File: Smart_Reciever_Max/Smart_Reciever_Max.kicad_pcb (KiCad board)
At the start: 2 copper layers, 112 x 81 mm, 66 parts, among them J1 String1, J10 String10, J11 String11, J12 String12, J13 RJ45, J14 VIN_Voltage, J15 PRG, J2 String2, J3 String3, J4 String4, J5 String5, J6 String6, J7 String7, J8 String8, J9 String9, SW1 SW_Push, U1 AMS1117-3.3, U2 L7805, U3 STM32F410CBTx, U4 AM26LV32xD, U5 74LS125, U6 74LS125, U7 74LS125

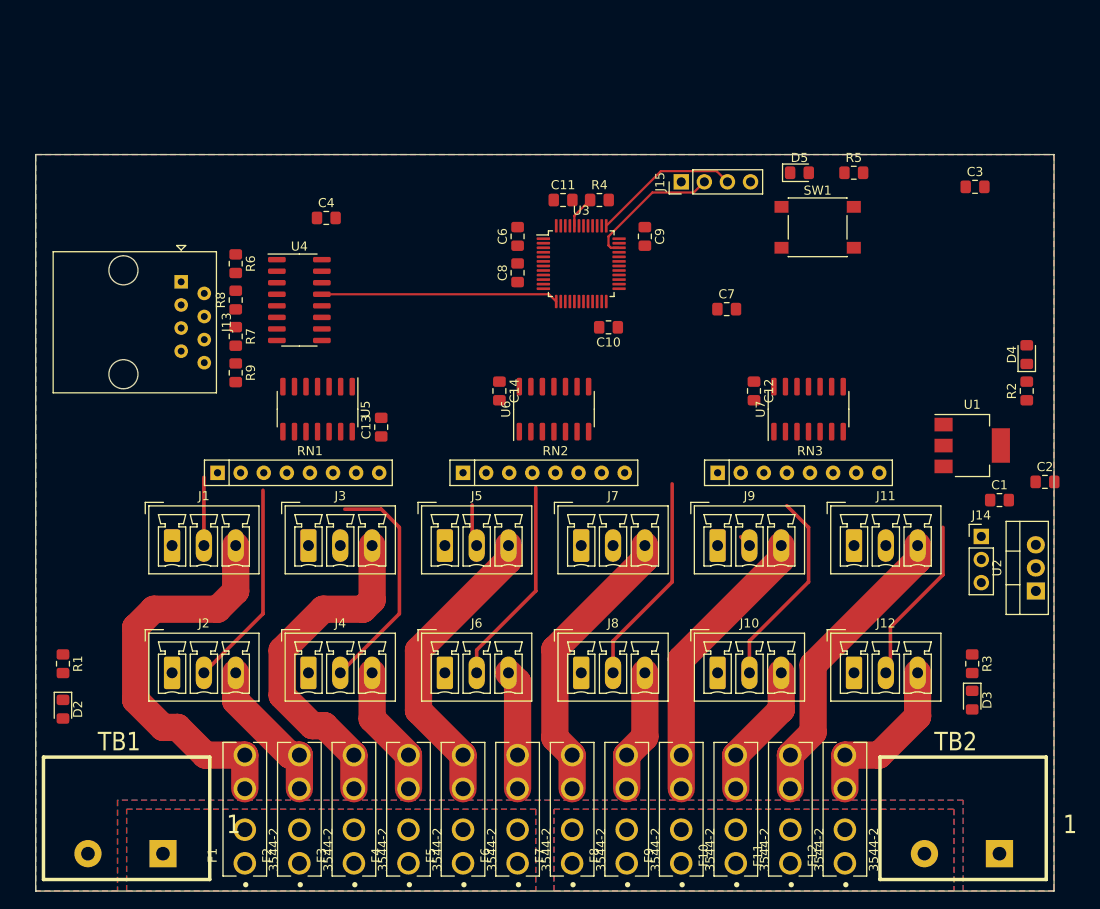
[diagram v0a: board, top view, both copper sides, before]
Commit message: Early Design of 12 port Smart Receiver. TODO: BOM, and clean up firmware for STM32L412
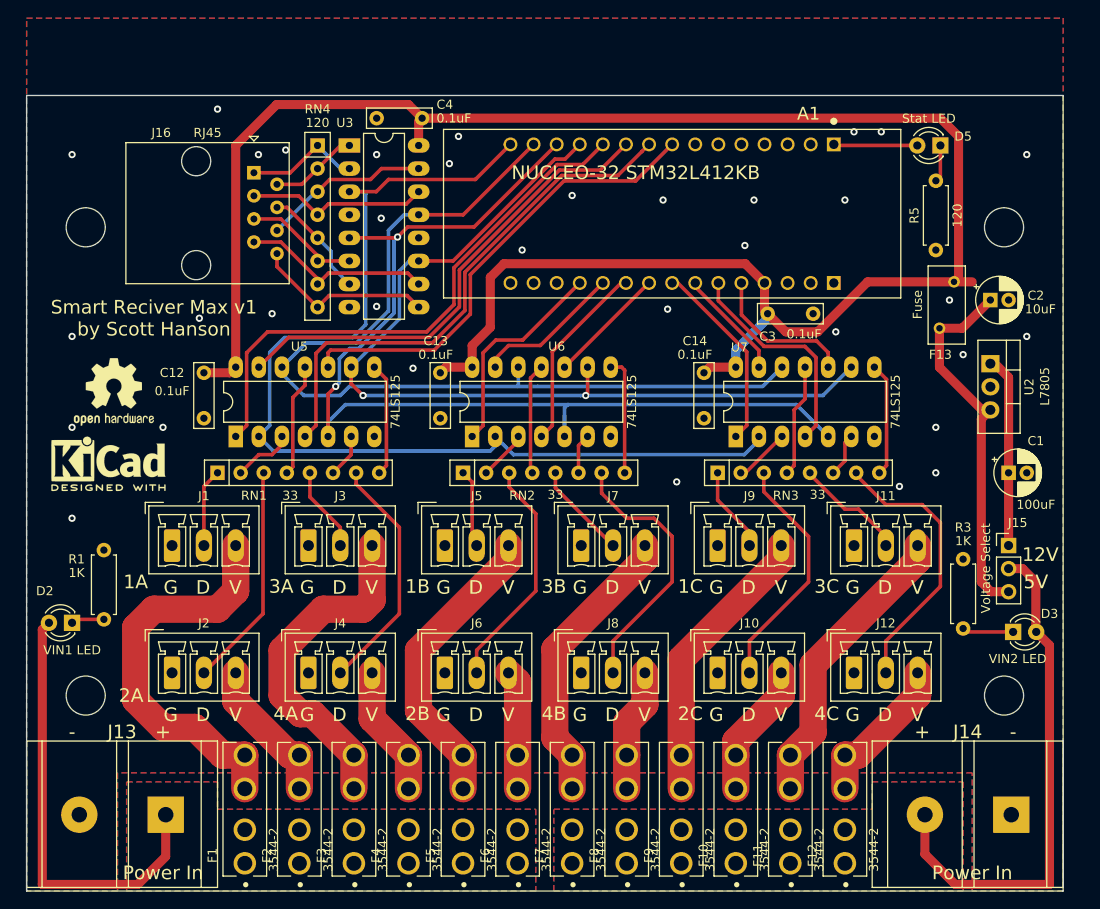
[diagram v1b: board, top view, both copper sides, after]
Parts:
- removed C10, C11, C6, C8, C9: 0.1uF, Capacitor_SMD:C_0805_2012Metric_Pad1.15x1.40mm_HandSolder
- removed C7: 4.7uF, Capacitor_SMD:C_0805_2012Metric_Pad1.15x1.40mm_HandSolder
- removed D4: 3.3V LED, LED_SMD:LED_0805_2012Metric_Pad1.15x1.40mm_HandSolder
- removed the J13 at (117.0, 89.0)
- removed the J15 at (172.0, 78.0)
- removed R2, R6, R7, R8, R9: 120, Resistor_SMD:R_0805_2012Metric_Pad1.15x1.40mm_HandSolder
- removed R4: 10K, Resistor_SMD:R_0805_2012Metric_Pad1.15x1.40mm_HandSolder
- removed SW1: SW_Push, Button_Switch_SMD:SW_Push_1P1T_NO_6x6mm_H9.5mm
- removed U1: AMS1117-3.3, Package_TO_SOT_SMD:SOT-223-3_TabPin2
- removed U4: AM26LV32xD, Package_SO:SOIC-16_3.9x9.9mm_P1.27mm
- added A1: NUCLEO-32 STM32L412KB, NUCLEO:MODULE_NUCLEO-F303K8, F.Cu at (171.0, 81.5)
- added F13: Fuse, Fuse:Fuse_BelFuse_0ZRE0005FF_L8.3mm_W3.8mm, F.Cu at (202.0, 89.0)
- added H1: MountingHole, MountingHole:MountingHole_4.3mm_M4, F.Cu at (106.5, 134.5)
- added H2: MountingHole, MountingHole:MountingHole_4.3mm_M4, F.Cu at (106.5, 83.0)
- added H3: MountingHole, MountingHole:MountingHole_4.3mm_M4, F.Cu at (207.5, 134.5)
- added H4: MountingHole, MountingHole:MountingHole_4.3mm_M4, F.Cu at (207.5, 83.0)
- added J16: RJ45, Connector_RJ:RJ45_Amphenol_54602-x08_Horizontal, F.Cu at (125.0, 77.0)
- added REF**: OSHW-Logo2_9.8x8mm_SilkScreen, Symbol:OSHW-Logo2_9.8x8mm_SilkScreen, F.Cu at (109.6, 101.1)
- added REF**: KiCad-Logo2_5mm_SilkScreen, Symbol:KiCad-Logo2_5mm_SilkScreen, F.Cu at (109.0, 109.0)
- added RN4: 120, Resistor_THT:R_Array_SIP8, F.Cu at (132.0, 74.0)
- C1: value 10uF -> 100uF; footprint Capacitor_SMD:C_0805_2012Metric_Pad1.15x1.40mm_HandSolder -> Capacitor_THT:CP_Radial_D5.0mm_P2.00mm
- C12, C13, C14, C4: footprint Capacitor_SMD:C_0805_2012Metric_Pad1.15x1.40mm_HandSolder -> Capacitor_THT:C_Rect_L7.0mm_W2.0mm_P5.00mm
- C2: footprint Capacitor_SMD:C_0805_2012Metric_Pad1.15x1.40mm_HandSolder -> Capacitor_THT:CP_Radial_D5.0mm_P2.00mm
- C3: value 10uF -> 0.1uF; footprint Capacitor_SMD:C_0805_2012Metric_Pad1.15x1.40mm_HandSolder -> Capacitor_THT:C_Rect_L7.0mm_W2.0mm_P5.00mm
- D2, D3, D5: footprint LED_SMD:LED_0805_2012Metric_Pad1.15x1.40mm_HandSolder -> LED_THT:LED_D3.0mm_Clear
- J13: renamed from TB1; footprint Barrier_Blocks:BARRIER_BLOCK_1ROW_2POS -> Barrier_Blocks:BARRIER_BLOCK_1ROW_2POS_P9.5MM
- J14: renamed from TB2; footprint Barrier_Blocks:BARRIER_BLOCK_1ROW_2POS -> Barrier_Blocks:BARRIER_BLOCK_1ROW_2POS_P9.5MM
- R1, R3, R5: footprint Resistor_SMD:R_0805_2012Metric_Pad1.15x1.40mm_HandSolder -> Resistor_THT:R_Axial_DIN0207_L6.3mm_D2.5mm_P7.62mm_Horizontal
- U3: value STM32F410CBTx -> AM26C32IN; footprint Package_QFP:LQFP-48_7x7mm_P0.5mm -> Package_DIP:DIP-16_W7.62mm_LongPads
- U5, U6, U7: footprint Package_SO:SOIC-14_3.9x8.7mm_P1.27mm -> Package_DIP:DIP-14_W7.62mm_LongPads
- moved C12 60.5 mm to (119.5, 99.0)
- moved U3 28.6 mm to (135.5, 74.0)
- moved C3 26.7 mm to (181.5, 92.5)
- moved U2 25.5 mm to (206.0, 98.0), turned to 270 degrees
- moved C14 22.6 mm to (174.5, 99.0)
- moved C2 20.9 mm to (206.0, 91.0)
- moved D5 15.8 mm to (200.5, 74.0), turned to 180 degrees
- moved C4 15.2 mm to (143.5, 71.0), turned to 180 degrees
- moved J14 13.9 mm to (214.0, 139.5)
- moved R1 13.3 mm to (108.5, 118.5)
- moved J13 13.1 mm to (121.0, 139.5)
- moved R5 12.4 mm to (200.0, 85.5), turned to 90 degrees
- moved R3 11.5 mm to (203.0, 119.5)
- moved D2 9.55 mm to (105.0, 126.5), turned to 180 degrees
- moved U5 9.49 mm to (123.0, 106.0), turned to 90 degrees
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- renumbered J14 to J15
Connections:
- C2 pad 1: +5V -> 5IN
- C3 pad 1: +3V3 -> +5V
- C4 pad 1: +3V3 -> +5V
- D5 pad 2: Net-(D5-Pad2) -> Net-(A1-Pad3.1)
- J15 pad 3: +5V -> 5IN
- RN2 pad 1: Net-(RN2-Pad1) -> /Outputs/DOUT5
- RN2 pad 2: /Outputs/DOUT5 -> Net-(RN2-Pad2)
- RN2 pad 3: Net-(RN2-Pad3) -> /Outputs/DOUT6
- RN2 pad 4: /Outputs/DOUT6 -> Net-(RN2-Pad4)
- RN2 pad 5: Net-(RN2-Pad5) -> /Outputs/DOUT7
- RN2 pad 6: /Outputs/DOUT7 -> Net-(RN2-Pad6)
- RN2 pad 7: Net-(RN2-Pad7) -> /Outputs/DOUT8
- RN2 pad 8: /Outputs/DOUT8 -> Net-(RN2-Pad8)
- RN3 pad 1: Net-(RN3-Pad1) -> /Outputs/DOUT9
- RN3 pad 2: /Outputs/DOUT9 -> Net-(RN3-Pad2)
- RN3 pad 3: Net-(RN3-Pad3) -> /Outputs/DOUT10
- RN3 pad 4: /Outputs/DOUT10 -> Net-(RN3-Pad4)
- RN3 pad 5: Net-(RN3-Pad5) -> /Outputs/DOUT11
- RN3 pad 6: /Outputs/DOUT11 -> Net-(RN3-Pad6)
- RN3 pad 7: Net-(RN3-Pad7) -> /Outputs/DOUT12
- RN3 pad 8: /Outputs/DOUT12 -> Net-(RN3-Pad8)
- U2 pad 3: +5V -> 5IN
- U3 pad 1: Net-(U3-Pad1) -> /Serial/Serial1_N
- U3 pad 10: DATA1 -> /Serial/Serial4_P
- U3 pad 11: DATA2 -> DATA4
- U3 pad 12: DATA3 -> GND
- U3 pad 13: DATA4 -> DATA2
- U3 pad 14: EN1A -> /Serial/Serial2_P
- U3 pad 15: EN2A -> /Serial/Serial2_N
- U3 pad 16: EN3A -> +5V
- U3 pad 2: Net-(U3-Pad2) -> /Serial/Serial1_P
- U3 pad 3: Net-(U3-Pad3) -> DATA1
- U3 pad 4: Net-(U3-Pad4) -> GND
- U3 pad 5: Net-(U3-Pad5) -> DATA3
- U3 pad 6: Net-(U3-Pad6) -> /Serial/Serial3_P
- U3 pad 7: Net-(C6-Pad1) -> /Serial/Serial3_N
- U3 pad 9: +3V3 -> /Serial/Serial4_N
- U5 pad 1: EN2A -> EN1A
- U5 pad 10: EN3A -> EN4A
- U5 pad 11: Net-(RN1-Pad8) -> Net-(RN1-Pad4)
- U5 pad 12: DATA4 -> DATA2
- U5 pad 13: EN4A -> EN2A
- U5 pad 2: DATA2 -> DATA1
- U5 pad 3: Net-(RN1-Pad4) -> Net-(RN1-Pad2)
- U5 pad 4: EN1A -> EN3A
- U5 pad 5: DATA1 -> DATA3
- U5 pad 6: Net-(RN1-Pad2) -> Net-(RN1-Pad6)
- U5 pad 8: Net-(RN1-Pad6) -> Net-(RN1-Pad8)
- U5 pad 9: DATA3 -> DATA4
- U6 pad 1: EN2B -> EN1B
- U6 pad 10: EN1B -> EN4B
- U6 pad 11: Net-(RN2-Pad7) -> Net-(RN2-Pad4)
- U6 pad 12: DATA4 -> DATA2
- U6 pad 13: EN4B -> EN2B
- U6 pad 2: DATA2 -> DATA1
- U6 pad 3: Net-(RN2-Pad3) -> Net-(RN2-Pad2)
- U6 pad 6: Net-(RN2-Pad5) -> Net-(RN2-Pad6)
- U6 pad 8: Net-(RN2-Pad1) -> Net-(RN2-Pad8)
- U6 pad 9: DATA1 -> DATA4
- U7 pad 1: EN2C -> EN1C
- U7 pad 10: EN1C -> EN4C
- U7 pad 11: Net-(RN3-Pad7) -> Net-(RN3-Pad4)
- U7 pad 12: DATA4 -> DATA2
- U7 pad 13: EN4C -> EN2C
- U7 pad 2: DATA2 -> DATA1
- U7 pad 3: Net-(RN3-Pad3) -> Net-(RN3-Pad2)
- U7 pad 6: Net-(RN3-Pad5) -> Net-(RN3-Pad6)
- U7 pad 8: Net-(RN3-Pad1) -> Net-(RN3-Pad8)
- U7 pad 9: DATA1 -> DATA4
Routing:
- net +5V: track 0.00 -> 216.2 mm
- net DATA3: track 0.00 -> 117.6 mm, vias 0 -> 2
- net DATA1: track 0.00 -> 117.2 mm
- net DATA2: track 0.00 -> 103.6 mm
- net DATA4: track 26.1 -> 100.2 mm, vias 0 -> 2
- net EN1A: track 0.00 -> 60.7 mm
- net EN3A: track 0.00 -> 58.2 mm
- net VIN2: track 0.00 -> 56.9 mm
- net EN2A: track 0.00 -> 52.9 mm
- net EN4A: track 0.00 -> 51.5 mm
- net VIN1: track 0.00 -> 48.5 mm
- net 5IN: track 0.00 -> 41.5 mm
- net EN3C: track 0.00 -> 24.5 mm
- net EN1B: track 0.00 -> 23.5 mm
- net EN1C: track 0.00 -> 21.5 mm
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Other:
- board size 112 x 81 mm -> 114 x 87.5 mm
- net class Default: trace_width 0.25 -> 0.4
- board text added: "+"
- board text added: "-"
- board text added: "12V"
- board text added: "1A"
- board text added: "1B"
- board text added: "1C"
- board text added: "2A"
- board text added: "2B"
- board text added: "2C"
- board text added: "3A"
- board text added: "3B"
- board text added: "3C"
- board text added: "4A"
- board text added: "4B"
- board text added: "4C"
- board text added: "5V"
- board text added: "D"
- board text added: "G"
- board text added: "Smart Reciver Max v1 by Scott Hanson"
- board text added: "V"
- board text added: "Voltage Select"

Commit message: porting Exp Max changes
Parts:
- removed D5: Stat LED, LED_THT:LED_D3.0mm_Clear
- removed REF**: OSHW-Logo2_9.8x8mm_SilkScreen, Symbol:OSHW-Logo2_9.8x8mm_SilkScreen
- removed REF**: KiCad-Logo2_5mm_SilkScreen, Symbol:KiCad-Logo2_5mm_SilkScreen
- added D3: Stat LED, LED_THT:LED_D3.0mm_Clear, F.Cu at (199.0, 75.5)
- added J17: EXT1, Connector_PinHeader_2.54mm:PinHeader_1x04_P2.54mm_Vertical, F.Cu at (173.5, 71.2)
- added R4: 10k, Resistor_THT:R_Axial_DIN0207_L6.3mm_D2.5mm_P7.62mm_Horizontal, F.Cu at (173.5, 87.2)
- added SW1: USR, Button_Switch_THT:SW_PUSH_6mm, F.Cu at (205.0, 71.5)
- added TP1: PC14, TestPoint:TestPoint_Pad_1.5x1.5mm, B.Cu at (164.0, 71.8)
- added TP2: PC15, TestPoint:TestPoint_Pad_1.5x1.5mm, B.Cu at (160.5, 71.8)
- added TP3: 3V3, TestPoint:TestPoint_Pad_1.5x1.5mm, B.Cu at (173.5, 83.2)
- added TP4: GND, TestPoint:TestPoint_Pad_1.5x1.5mm, B.Cu at (184.0, 83.2)
- A1: value NUCLEO-32 STM32L412KB -> NUCLEO-L412KB; footprint NUCLEO:MODULE_NUCLEO-F303K8 -> NUCLEO:MODULE_NUCLEO-L412KB
- F13: value Fuse -> 500mA
- U3: renamed from U5; value 74LS125 -> 74HC125
- U4: renamed from U6; value 74LS125 -> 74HC125
- U5: renamed from U7; value 74LS125 -> 74HC125
- moved R1 5.24 mm to (105.0, 114.6)
- moved R3 2.76 mm to (198.0, 87.4)
- moved A1 2.65 mm to (168.5, 82.4)
- moved F13 2.25 mm to (202.0, 91.2)
- moved C3 0.90 mm to (182.0, 93.2)
- moved C2 0.90 mm to (206.0, 91.9)
- renumbered C12 to C5, C13 to C6, C14 to C7, D2 to D1, D3 to D2, R3 to R2, R5 to R3, U2 to U1, U3 to U2
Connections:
- A1 pad 3.10: EN2A -> PC14
- A1 pad 3.11: EN1A -> PC15
- A1 pad 3.2: Net-(A1-Pad3.2) -> PA10
- A1 pad 3.5: Net-(A1-Pad3.5) -> PA12
- A1 pad 3.6: Net-(A1-Pad3.6) -> EN4A
- A1 pad 3.7: Net-(A1-Pad3.7) -> EN3A
- A1 pad 3.8: EN4A -> EN2A
- A1 pad 3.9: EN3A -> EN1A
- A1 pad 4.15: Net-(A1-Pad4.15) -> PB3
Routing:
- net PB3: track 0.00 -> 40.0 mm, vias 0 -> 2
- net PA10: track 0.00 -> 30.9 mm, vias 0 -> 1
- net +3V3: track 0.00 -> 26.0 mm
- net PA12: track 0.00 -> 3.54 mm
- net DATA1: track 117.2 -> 113.7 mm
- net 5IN: track 41.5 -> 38.2 mm
- net PC14: track 0.00 -> 3.25 mm
- net EN2B: track 16.6 -> 13.4 mm
- net PC15: track 0.00 -> 3.17 mm
- net EN1A: track 60.7 -> 63.6 mm
- net EN2A: track 52.9 -> 55.8 mm
- net DATA4: track 100.2 -> 97.4 mm
- net DATA3: track 117.6 -> 114.7 mm
- net DATA2: track 103.6 -> 100.8 mm
- net EN3A: track 58.2 -> 61.0 mm
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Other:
- board text added: "GND"
- board text added: "PA12"
- board text added: "PB3"
